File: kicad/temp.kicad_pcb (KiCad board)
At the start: 2 copper layers, 24 parts, among them J1 Conn_01x06_Male, J10 Conn_01x01_Female, J11 Conn_01x01_Female, J12 Conn_01x01_Female, J13 Conn_01x01_Female, J14 Conn_01x01_Female, J15 Conn_01x01_Female, J16 Conn_01x01_Female, J2 Conn_01x02_Female, J3 Conn_01x01_Female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

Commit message: add accel pcb
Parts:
- added C2: C, Capacitor_THT:C_Rect_L7.0mm_W3.5mm_P2.50mm_P5.00mm, F.Cu at (66.7, 97.2)
- added C4: C, Capacitor_THT:C_Rect_L7.0mm_W3.5mm_P2.50mm_P5.00mm, F.Cu at (66.0, 87.6)
- added J17: Conn_01x01_Male, Connector_PinHeader_2.54mm:PinHeader_1x01_P2.54mm_Vertical, F.Cu at (52.7, 83.2)
- added J18: Conn_01x05_Male, Connector_PinHeader_2.54mm:PinHeader_1x05_P2.54mm_Vertical, F.Cu at (48.3, 85.7)
- added J19: Conn_01x01_Male, Connector_PinHeader_2.54mm:PinHeader_1x01_P2.54mm_Vertical, F.Cu at (52.7, 95.9)
- added J20: Conn_01x01_Male, Connector_PinHeader_2.54mm:PinHeader_1x01_P2.54mm_Vertical, F.Cu at (74.9, 92.7)
- added J21: Conn_01x01_Male, Connector_PinHeader_2.54mm:PinHeader_1x01_P2.54mm_Vertical, F.Cu at (74.9, 87.6)
- added R2: R, Resistor_THT:R_Axial_DIN0207_L6.3mm_D2.5mm_P10.16mm_Horizontal, F.Cu at (62.2, 87.6)
- added R3: R, Resistor_THT:R_Axial_DIN0207_L6.3mm_D2.5mm_P10.16mm_Horizontal, F.Cu at (62.2, 91.4)

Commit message: kortslut modul
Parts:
- added J22: Conn_01x03_Male, Connector_PinHeader_2.54mm:PinHeader_1x03_P2.54mm_Vertical, F.Cu at (65.4, 107.9)
- added Q2: TIP120, Package_TO_SOT_THT:TO-220-3_Vertical, F.Cu at (59.1, 108.0)
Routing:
- net Earth: track 120.0 -> 143.5 mm
- net Net-(C4-Pad2): track 0.00 -> 18.9 mm
- net Net-(C2-Pad2): track 0.00 -> 14.5 mm
- net Net-(J22-Pad3): track 0.00 -> 6.42 mm
- net Net-(J22-Pad1): track 0.00 -> 6.42 mm
- net Coll: track 0.00 -> 6.42 mm
- net Net-(J17-Pad1): track 0.00 -> 5.50 mm
- net Net-(J18-Pad2): track 0.00 -> 4.07 mm
- net Net-(J18-Pad3): track 0.00 -> 4.07 mm

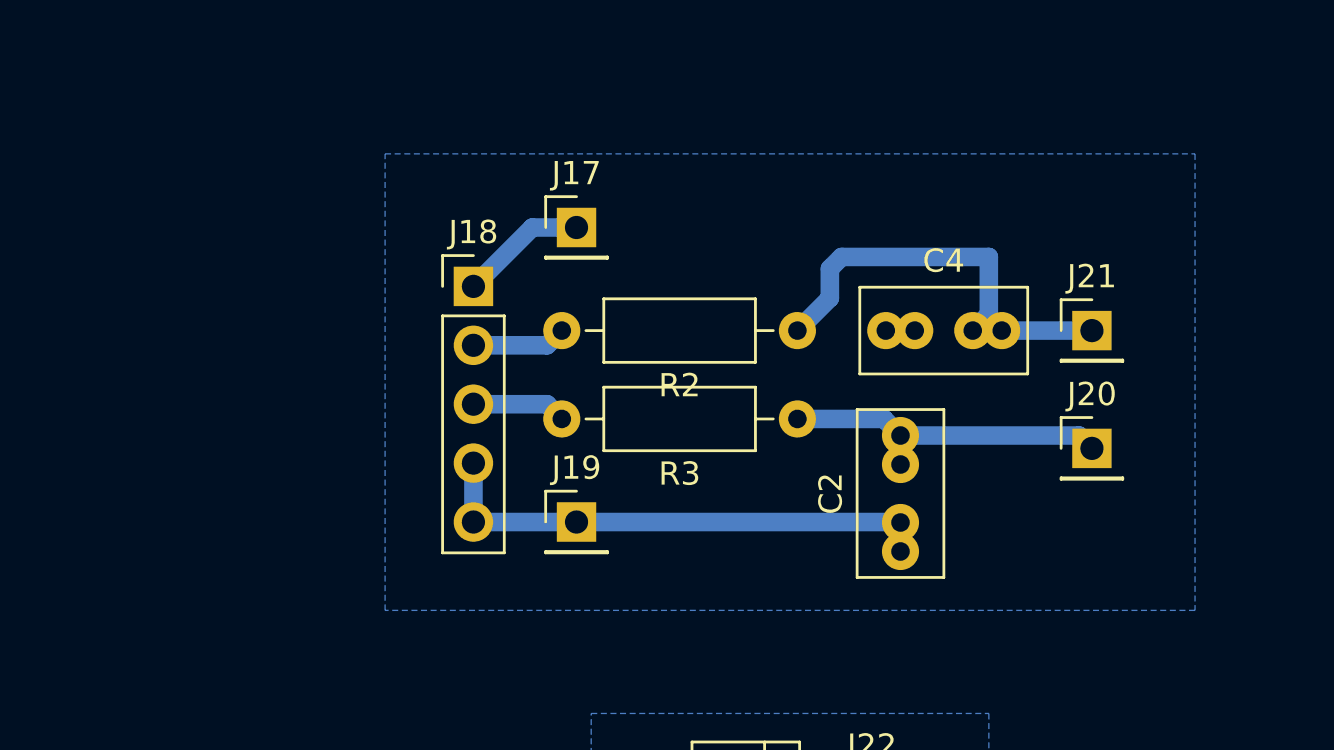
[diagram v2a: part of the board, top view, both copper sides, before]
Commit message: 12-3.3V converter
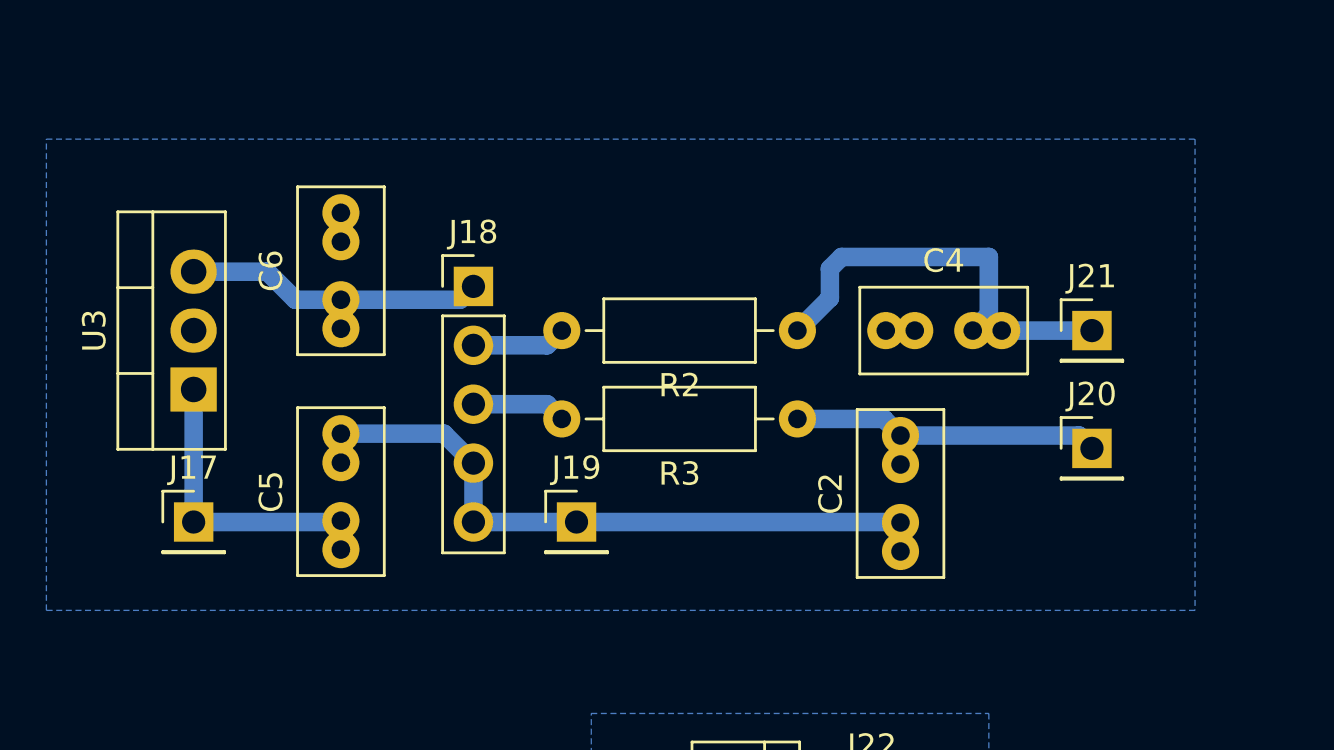
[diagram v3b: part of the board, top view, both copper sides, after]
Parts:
- added C5: C, Capacitor_THT:C_Rect_L7.0mm_W3.5mm_P2.50mm_P5.00mm, F.Cu at (42.5, 97.1)
- added C6: C, Capacitor_THT:C_Rect_L7.0mm_W3.5mm_P2.50mm_P5.00mm, F.Cu at (42.5, 87.5)
- added U3: LM7805_TO220, Package_TO_SOT_THT:TO-220-3_Vertical, F.Cu at (36.2, 90.2)
- moved J17 20.8 mm to (36.2, 95.9)
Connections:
- J17 pad 1: Net-(J17-Pad1) -> Power
- J18 pad 1: Net-(J17-Pad1) -> 3.3V
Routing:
- net 3.3V: track 0.00 -> 14.1 mm
- net Power: track 0.00 -> 13.3 mm
- net Earth: track 143.5 -> 152.2 mm
- net Net-(J17-Pad1): track 5.50 -> 0.00 mm
